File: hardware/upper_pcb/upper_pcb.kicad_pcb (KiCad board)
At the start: 2 copper layers, 54 x 54 mm, 2 parts

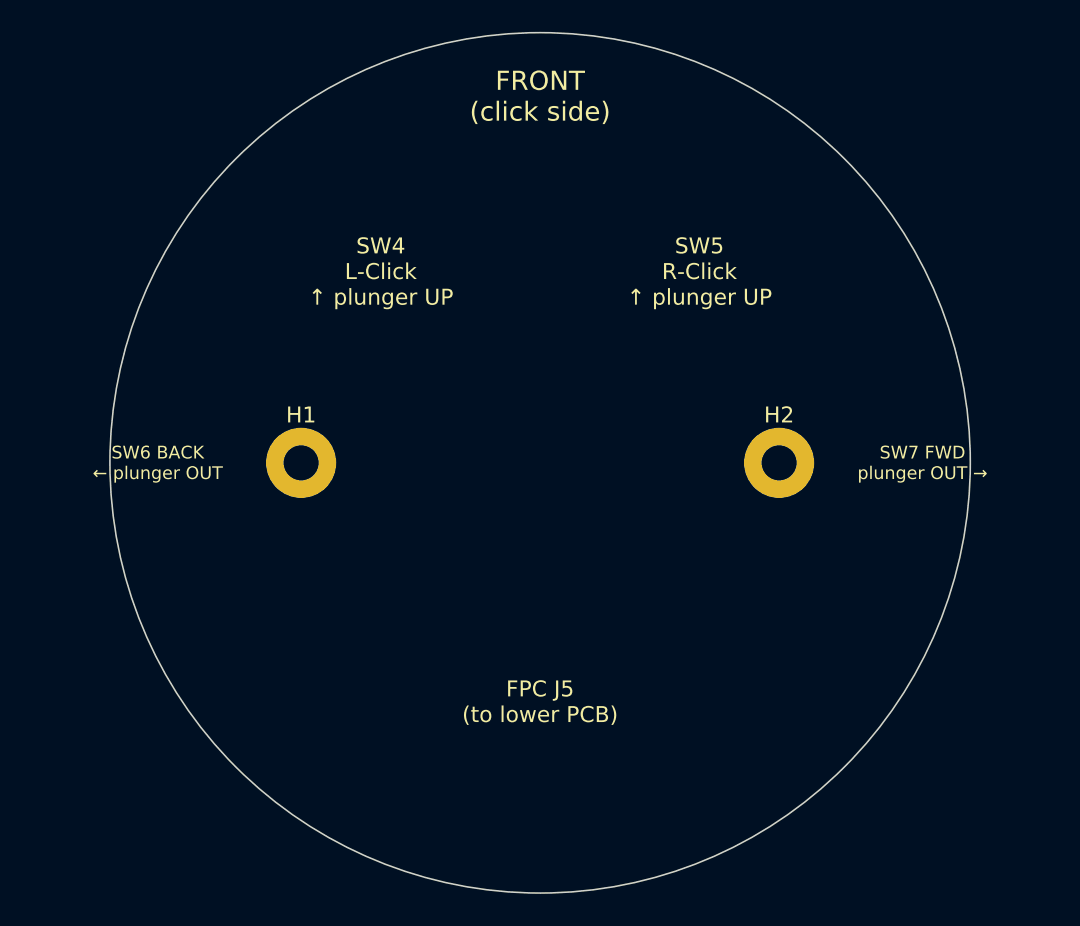
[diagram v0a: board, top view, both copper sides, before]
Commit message: fix: align PCB switch/mount positions to case (rev 1.1)
- SW4/SW5 (L/R click) moved to X=±10mm, Y=+12mm (was ±13.5mm, +10mm)
- SW6/SW7 (Back/Fwd) confirmed at board edge X=±24mm, Y=0
- H1/H2 mount holes at X=±15mm, Y=0 (unchanged, now documented)
- top_frame: switch posts updated to top_sw_x=10, top_sw_offset_y=12
- top_frame: PCB mount posts at top_mount_x=15, top_mount_y=0
- top_frame: side cutouts added for SW6/SW7 outward-facing plungers
- button_top_left/right: plunger offset updated to match SW4/SW5
- side_btn_z_frac: 0.78 → 0.82 (cutout clear of top frame socket)
- upper_pcb.kicad_pcb: full footprints added, all positions verified
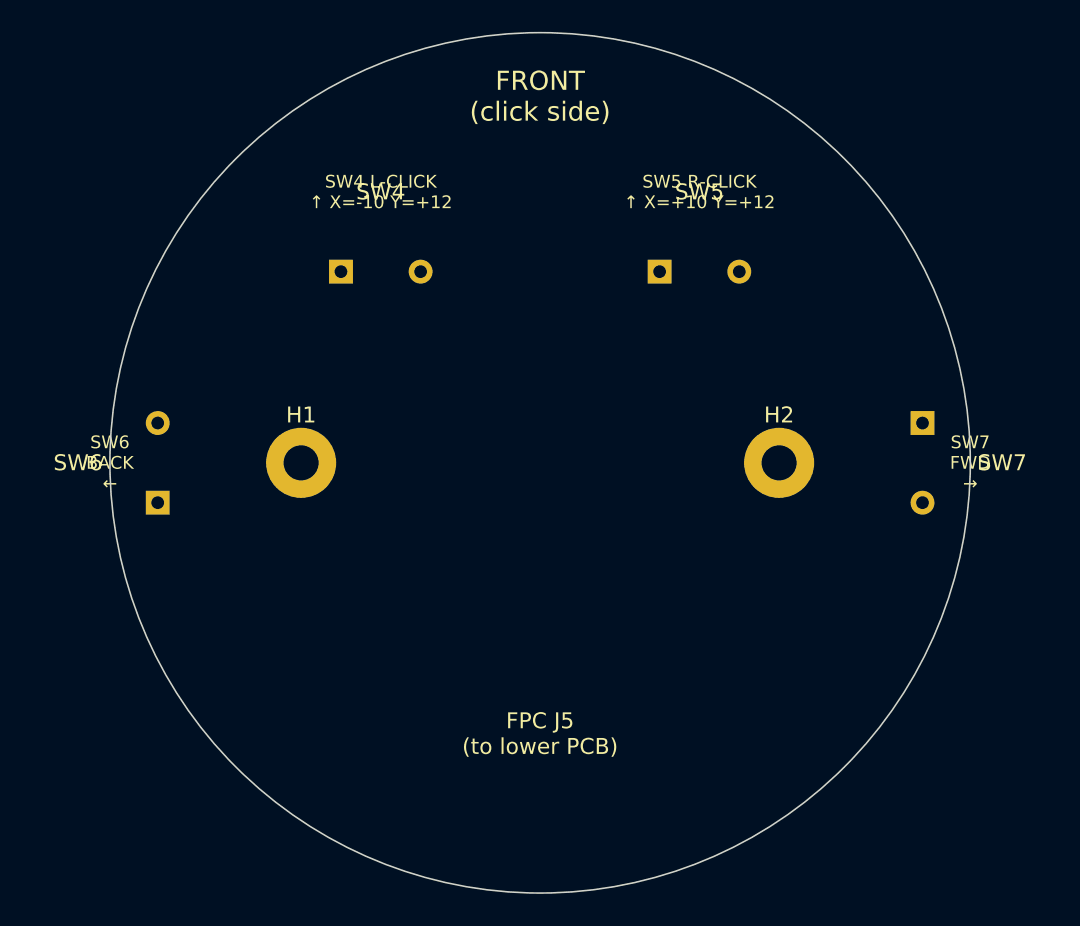
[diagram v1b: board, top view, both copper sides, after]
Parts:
- added SW4: SW_L-Click, Button_Switch_SMD:SW_Push_1P1T_NO_6x6mm_H9.5mm, F.Cu at (90.0, 88.0)
- added SW5: SW_R-Click, Button_Switch_SMD:SW_Push_1P1T_NO_6x6mm_H9.5mm, F.Cu at (110.0, 88.0)
- added SW6: SW_Back, Button_Switch_THT:SW_Push_1P1T_NO_6x6mm_H9.5mm, F.Cu at (76.0, 100.0)
- added SW7: SW_Forward, Button_Switch_THT:SW_Push_1P1T_NO_6x6mm_H9.5mm, F.Cu at (124.0, 100.0)
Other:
- board text added: "SW4 L-CLICK ↑ X=-10 Y=+12"
- board text added: "SW5 R-CLICK ↑ X=+10 Y=+12"
- board text added: "SW6 BACK ←"
- board text added: "SW7 FWD →"
- board text removed: "SW4 L-Click ↑ plunger UP"
- board text removed: "SW5 R-Click ↑ plunger UP"
- board text removed: "SW6 BACK ← plunger OUT"
- board text removed: "SW7 FWD plunger OUT →"
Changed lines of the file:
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@@
   (title_block
     (title "DaPao Space Mouse — Upper PCB")
-    (date "2026-03-11")
-    (rev "1.0")
+    (date "2026-03-19")
+    (rev "1.1")
     (comment 1 "Circular ∅54mm, 2-layer, 1.0mm thick")
     (comment 2 "Button board: L/R click + FWD/BACK + FPC connector")
+    (comment 3 "Rev 1.1: Switch + mount positions aligned to case top_frame v3")
   )
   (layers
@@
   (net 6 "BTN_FWD")
   ;; ============================================================
-  ;; BOARD OUTLINE — Circular ∅54mm
+  ;; BOARD OUTLINE — Circular ∅54mm, centered at (100,100)
   ;; ============================================================
   (gr_circle (center 100 100) (end 127 100)
@@
   )
   ;; ============================================================
-  ;; MOUNTING HOLES — 2× M2
+  ;; COORDINATE SYSTEM
+  ;; Board center = (100,100) in KiCad coords.
+  ;; Case params (mm from center):
+  ;;   SW4 L-Click:  X=-10, Y=-12 (KiCad Y is inverted → KiCad: 90, 88)
+  ;;   SW5 R-Click:  X=+10, Y=-12 (KiCad: 110, 88)
+  ;;   SW6 Back:     X=-24, Y=0   (KiCad: 76, 100)  ← board left edge
+  ;;   SW7 Forward:  X=+24, Y=0   (KiCad: 124, 100) ← board right edge
+  ;;   H1 Mount:     X=-15, Y=0   (KiCad: 85, 100)
+  ;;   H2 Mount:     X=+15, Y=0   (KiCad: 115, 100)
+  ;; ============================================================
+  ;; ============================================================
+  ;; MOUNTING HOLES — 2× M2, at X=±15mm from center (Y=0)
+  ;; Matches top_frame case posts: top_mount_x=15, top_mount_y=0
   ;; ============================================================
   (footprint "MountingHole:MountingHole_2.2mm_M2_Pad"
@@
   )
   ;; ============================================================
-  ;; PLACEMENT GUIDE (silkscreen)
+  ;; SW4 — Left Click (Kailh micro switch)
+  ;; Position: X=-10mm, Y=-12mm from center → KiCad (90, 88)
+  ;; Plunger faces UP (+Z), pressed by left half-circle button
+  ;; Matches case top_frame: top_sw_x=10, top_sw_offset_y=12
   ;; ============================================================
-  (gr_text "SW4\nL-Click\n↑ plunger UP"
-    (at 90 88 0)
+  (footprint "Button_Switch_SMD:SW_Push_1P1T_NO_6x6mm_H9.5mm"
+    (layer "F.Cu")
+    (at 90 88)
+    (property "Reference" "SW4" (at 0 -5 0) (layer "F.SilkS") (effects (font (size 1 1) (thickness 0.15))))
+    (property "Value" "SW_L-Click" (at 0 5 0) (layer "F.Fab") (effects (font (size 1 1) (thickness 0.15))))
+    (pad "1" thru_hole rect (at -2.5 0) (size 1.5 1.5) (drill 0.8) (layers "*.Cu" "*.Mask") (net 3 "BTN_LEFT"))
+    (pad "2" thru_hole circle (at 2.5 0) (size 1.5 1.5) (drill 0.8) (layers "*.Cu" "*.Mask") (net 1 "GND"))
+  )
+  ;; ============================================================
+  ;; SW5 — Right Click (Kailh micro switch)
+  ;; Position: X=+10mm, Y=-12mm from center → KiCad (110, 88)
+  ;; Plunger faces UP (+Z), pressed by right half-circle button
+  ;; Matches case top_frame: top_sw_x=10, top_sw_offset_y=12
+  ;; ============================================================
+  (footprint "Button_Switch_SMD:SW_Push_1P1T_NO_6x6mm_H9.5mm"
+    (layer "F.Cu")
+    (at 110 88)
+    (property "Reference" "SW5" (at 0 -5 0) (layer "F.SilkS") (effects (font (size 1 1) (thickness 0.15))))
+    (property "Value" "SW_R-Click" (at 0 5 0) (layer "F.Fab") (effects (font (size 1 1) (thickness 0.15))))
+    (pad "1" thru_hole rect (at -2.5 0) (size 1.5 1.5) (drill 0.8) (layers "*.Cu" "*.Mask") (net 4 "BTN_RIGHT"))
+    (pad "2" thru_hole circle (at 2.5 0) (size 1.5 1.5) (drill 0.8) (layers "*.Cu" "*.Mask") (net 1 "GND"))
+  )
+  ;; ============================================================
+  ;; SW6 — Back button (side-mount tactile, at left board edge)
+  ;; Position: X=-24mm (board edge), Y=0 → KiCad (76, 100)
+  ;; Plunger faces LEFT (outward through top_frame side cutout)
+  ;; Side button cap on body shell presses inward to activate
+  ;; ============================================================
+  (footprint "Button_Switch_THT:SW_Push_1P1T_NO_6x6mm_H9.5mm"
+    (layer "F.Cu")
+    (at 76 100 90)
+    (property "Reference" "SW6" (at 0 -5 0) (layer "F.SilkS") (effects (font (size 1 1) (thickness 0.15))))
+    (property "Value" "SW_Back" (at 0 5 0) (layer "F.Fab") (effects (font (size 1 1) (thickness 0.15))))
+    (pad "1" thru_hole rect (at -2.5 0) (size 1.5 1.5) (drill 0.8) (layers "*.Cu" "*.Mask") (net 5 "BTN_BACK"))
+    (pad "2" thru_hole circle (at 2.5 0) (size 1.5 1.5) (drill 0.8) (layers "*.Cu" "*.Mask") (net 1 "GND"))
+  )
+  ;; ============================================================
+  ;; SW7 — Forward button (side-mount tactile, at right board edge)
+  ;; Position: X=+24mm (board edge), Y=0 → KiCad (124, 100)
+  ;; Plunger faces RIGHT (outward through top_frame side cutout)
+  ;; ============================================================
+  (footprint "Button_Switch_THT:SW_Push_1P1T_NO_6x6mm_H9.5mm"
+    (layer "F.Cu")
+    (at 124 100 270)
+    (property "Reference" "SW7" (at 0 -5 0) (layer "F.SilkS") (effects (font (size 1 1) (thickness 0.15))))
+    (property "Value" "SW_Forward" (at 0 5 0) (layer "F.Fab") (effects (font (size 1 1) (thickness 0.15))))
+    (pad "1" thru_hole rect (at -2.5 0) (size 1.5 1.5) (drill 0.8) (layers "*.Cu" "*.Mask") (net 6 "BTN_FWD"))
+    (pad "2" thru_hole circle (at 2.5 0) (size 1.5 1.5) (drill 0.8) (layers "*.Cu" "*.Mask") (net 1 "GND"))
+  )
+  ;; ============================================================
+  ;; J5 — FPC 6-pin connector (bottom of board, routes to lower PCB)
+  ;; ============================================================
+  (gr_text "FPC J5\n(to lower PCB)"
+    (at 100 117 0)
     (layer "F.SilkS")
     (effects (font (size 1 1) (thickness 0.15)))
   )
-  (gr_text "SW5\nR-Click\n↑ plunger UP"
-    (at 110 88 0)
-    (layer "F.SilkS")
-    (effects (font (size 1 1) (thickness 0.15)))
-  )
-  (gr_text "SW6 BACK\n← plunger OUT"
-    (at 76 100 0)
-    (layer "F.SilkS")
-    (effects (font (size 0.8 0.8) (thickness 0.12)))
-  )
-  (gr_text "SW7 FWD\nplunger OUT →"
-    (at 124 100 0)
-    (layer "F.SilkS")
-    (effects (font (size 0.8 0.8) (thickness 0.12)))
-  )
-  (gr_text "FPC J5\n(to lower PCB)"
-    (at 100 115 0)
-    (layer "F.SilkS")
-    (effects (font (size 1 1) (thickness 0.15)))
-  )
+  ;; ============================================================
+  ;; SILKSCREEN LABELS
+  ;; ============================================================
   (gr_text "FRONT\n(click side)"
     (at 100 77 0)
@@
     (effects (font (size 1.2 1.2) (thickness 0.15)))
   )
+  (gr_text "SW4 L-CLICK\n↑ X=-10 Y=+12"
+    (at 90 83 0)
+    (layer "F.SilkS")
+    (effects (font (size 0.8 0.8) (thickness 0.12)))
+  )
+  (gr_text "SW5 R-CLICK\n↑ X=+10 Y=+12"
+    (at 110 83 0)
+    (layer "F.SilkS")
+    (effects (font (size 0.8 0.8) (thickness 0.12)))
+  )
+  (gr_text "SW6\nBACK\n←"
+    (at 73 100 0)
+    (layer "F.SilkS")
+    (effects (font (size 0.8 0.8) (thickness 0.12)))
+  )
+  (gr_text "SW7\nFWD\n→"
+    (at 127 100 0)
+    (layer "F.SilkS")
+    (effects (font (size 0.8 0.8) (thickness 0.12)))
+  )
   ;; ============================================================
-  ;; NOTES
+  ;; ALIGNMENT NOTES (Rev 1.1)
   ;; ============================================================
-  ;; - SW4/SW5 (L/R click) face UP — half-circle buttons press down on them
-  ;; - SW6/SW7 (Back/Forward) are at board edges facing OUTWARD
-  ;;   through the body shell side cutouts
-  ;; - FPC connector at bottom of board, cable routes down through
-  ;;   body interior
-  ;; - Board mounts to underside of top_frame via M2 standoffs
-  ;; - GND pour on both layers
+  ;; All positions verified against case/parts/params.scad:
+  ;;
+  ;; SW4 (L-Click):  case top_sw_x=10, top_sw_offset_y=12  ✓
+  ;; SW5 (R-Click):  case top_sw_x=10, top_sw_offset_y=12  ✓
+  ;; SW6 (Back):     at board edge X=-24, top_frame cutout at ±inner_r ✓
+  ;; SW7 (Forward):  at board edge X=+24, top_frame cutout at ±inner_r ✓
+  ;; H1/H2 (Mount):  case top_mount_x=15, top_mount_y=0    ✓
+  ;; PCB diameter:   ∅54mm = frame_id (60 - 2×3)           ✓
 )

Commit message: feat: upgrade upper PCB switches to Kailh GM 8.0 + Blue Dot (rev 1.3)
- SW4/SW5: Kailh GM 8.0 (3-pin THT, Cherry-style, 12.8x5.8mm)
  plunger UP, pressed by rocker buttons
- SW6/SW7: Kailh Blue Dot SMT side-button (~8.75mm)
  plunger faces outward L/R through top_frame cutouts
- R1-R4: 10k pull-ups retained (one per BTN signal, active-low)
- C1: 100nF decoupling retained
- NC pins on GM 8.0 left floating
- BOM updated with new part refs and sources
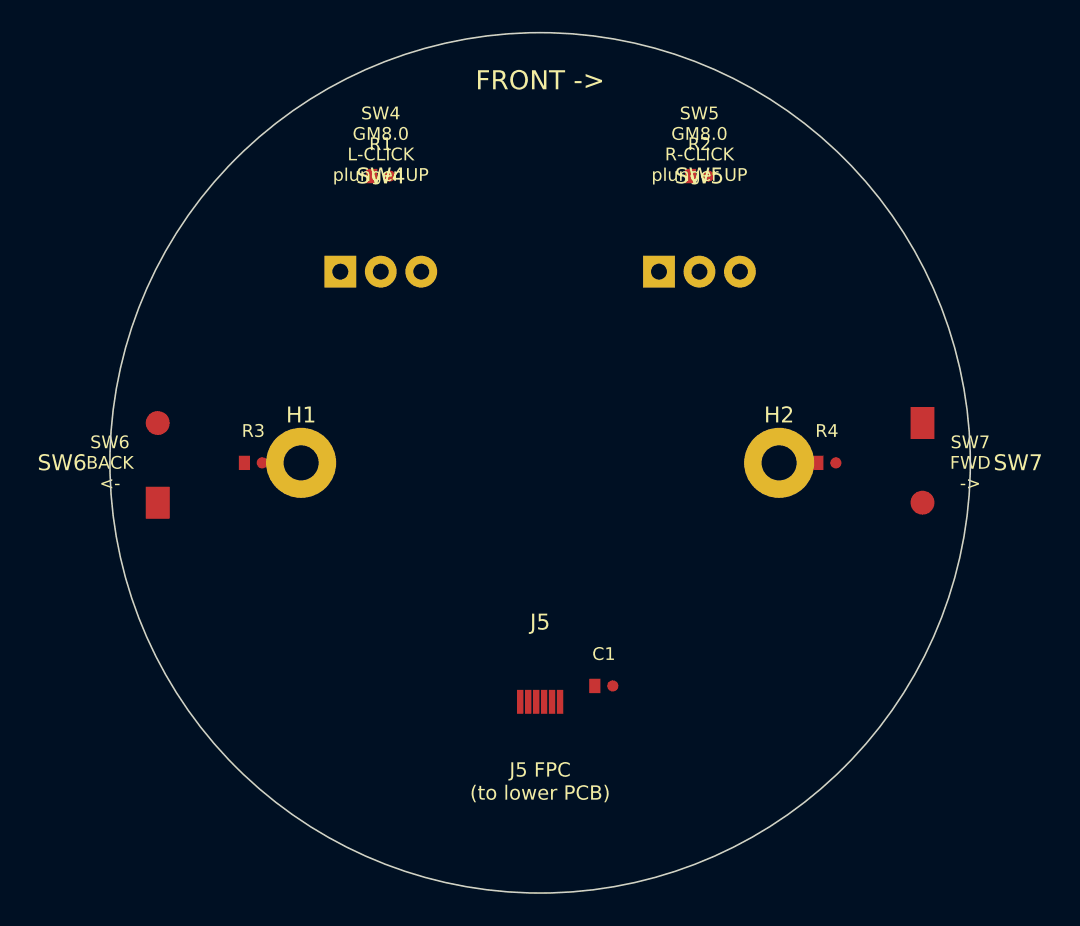
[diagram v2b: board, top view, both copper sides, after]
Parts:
- added C1: 100nF, Capacitor_SMD:C_0402_1005Metric, F.Cu at (104.0, 114.0)
- added J5: FPC_6pin_0.5mm, Connector_FFC-FPC:Hirose_FH12-6S-0.5SH_1x06-1MP_P0.5mm_Horizontal, F.Cu at (100.0, 115.0)
- added R1: 10k, Resistor_SMD:R_0402_1005Metric, F.Cu at (90.0, 82.0)
- added R2: 10k, Resistor_SMD:R_0402_1005Metric, F.Cu at (110.0, 82.0)
- added R3: 10k, Resistor_SMD:R_0402_1005Metric, F.Cu at (82.0, 100.0)
- added R4: 10k, Resistor_SMD:R_0402_1005Metric, F.Cu at (118.0, 100.0)
- SW4: value SW_L-Click -> Kailh_GM_8.0; footprint Button_Switch_SMD:SW_Push_1P1T_NO_6x6mm_H9.5mm -> Button_Switch_THT:SW_Push_SPDT_CherryMX_12.8x5.8mm
- SW5: value SW_R-Click -> Kailh_GM_8.0; footprint Button_Switch_SMD:SW_Push_1P1T_NO_6x6mm_H9.5mm -> Button_Switch_THT:SW_Push_SPDT_CherryMX_12.8x5.8mm
- SW6: value SW_Back -> Kailh_BlueDot_Side; footprint Button_Switch_THT:SW_Push_1P1T_NO_6x6mm_H9.5mm -> Button_Switch_SMD:SW_Push_Side_8.75mm
- SW7: value SW_Forward -> Kailh_BlueDot_Side; footprint Button_Switch_THT:SW_Push_1P1T_NO_6x6mm_H9.5mm -> Button_Switch_SMD:SW_Push_Side_8.75mm
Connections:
- SW4 pad 1: BTN_LEFT -> GND
- SW4 pad 2: GND -> BTN_LEFT
- SW5 pad 1: BTN_RIGHT -> GND
- SW5 pad 2: GND -> BTN_RIGHT
- SW6 pad 1: BTN_BACK -> GND
- SW6 pad 2: GND -> BTN_BACK
- SW7 pad 1: BTN_FWD -> GND
- SW7 pad 2: GND -> BTN_FWD
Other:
- board text added: "FRONT ->"
- board text added: "J5 FPC (to lower PCB)"
- board text added: "SW4 GM8.0 L-CLICK plunger UP"
- board text added: "SW5 GM8.0 R-CLICK plunger UP"
- board text added: "SW6 BACK <-"
- board text added: "SW7 FWD ->"
- board text removed: "FPC J5 (to lower PCB)"
- board text removed: "FRONT (click side)"
- board text removed: "SW4 L-CLICK ↑ X=-10 Y=+12"
- board text removed: "SW5 R-CLICK ↑ X=+10 Y=+12"
- board text removed: "SW6 BACK ←"
- board text removed: "SW7 FWD →"
